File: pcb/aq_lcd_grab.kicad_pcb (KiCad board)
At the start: 4 copper layers, 32 x 50 mm, 39 parts, among them J1 FH26W-39S-0.3SHW(60), J2 FH26W-39S-0.3SHW(60), J3 Conn_01x03_Socket, J4 Conn_01x02_Socket, J5 Conn_01x03_Pin, U1 STM32F103C8T6, U2 Conn_01x14

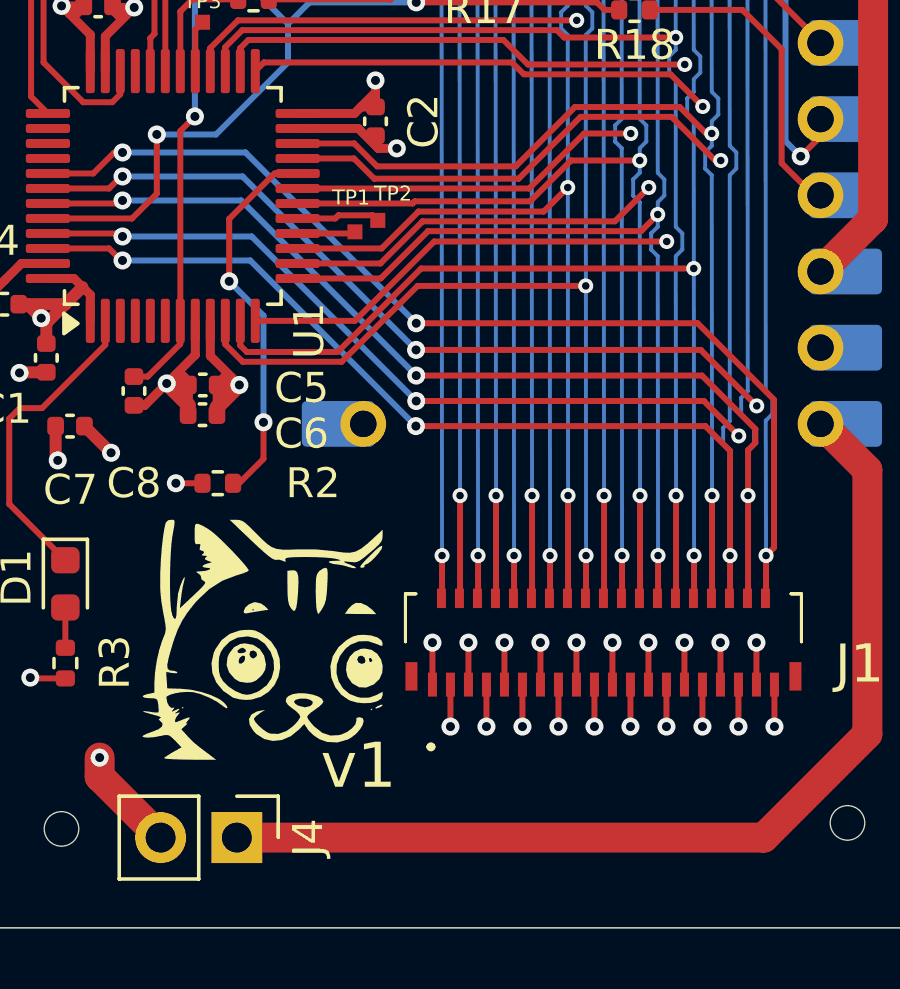
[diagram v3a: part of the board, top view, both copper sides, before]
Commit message: pcb: v2 — fix WR/CS swap on flex pins 22/24
The SKiDL pin map still carried the early probed pinout (22 = WR,
24 = CS); the module datasheet (docs/display_notes.md) has 22 = CS,
24 = WR. v1 therefore clocks TIM2_ETR (PA0) with CS instead of WR.

- aq_lcd_grab.py / .net / route_lcd_bus.py: swap pins 22 and 24.
- kicad_pcb: move the PA0/PA5 tap vias across the pin-22/24 columns,
  mirror the In2.Cu kinks of DC/P21/P25 around the new via spots,
  refill zones, relabel silkscreen v1 -> v2. DRC clean.
- pcb_spec.md: correct pinout table; add "v1 errata" describing the
  bodge wire (J2 "CS" pad -> U1 pin 10/PA0) for built v1 boards.

Co-Authored-By: Claude Opus 5.5 (1M context) <noreply@anthropic.com>
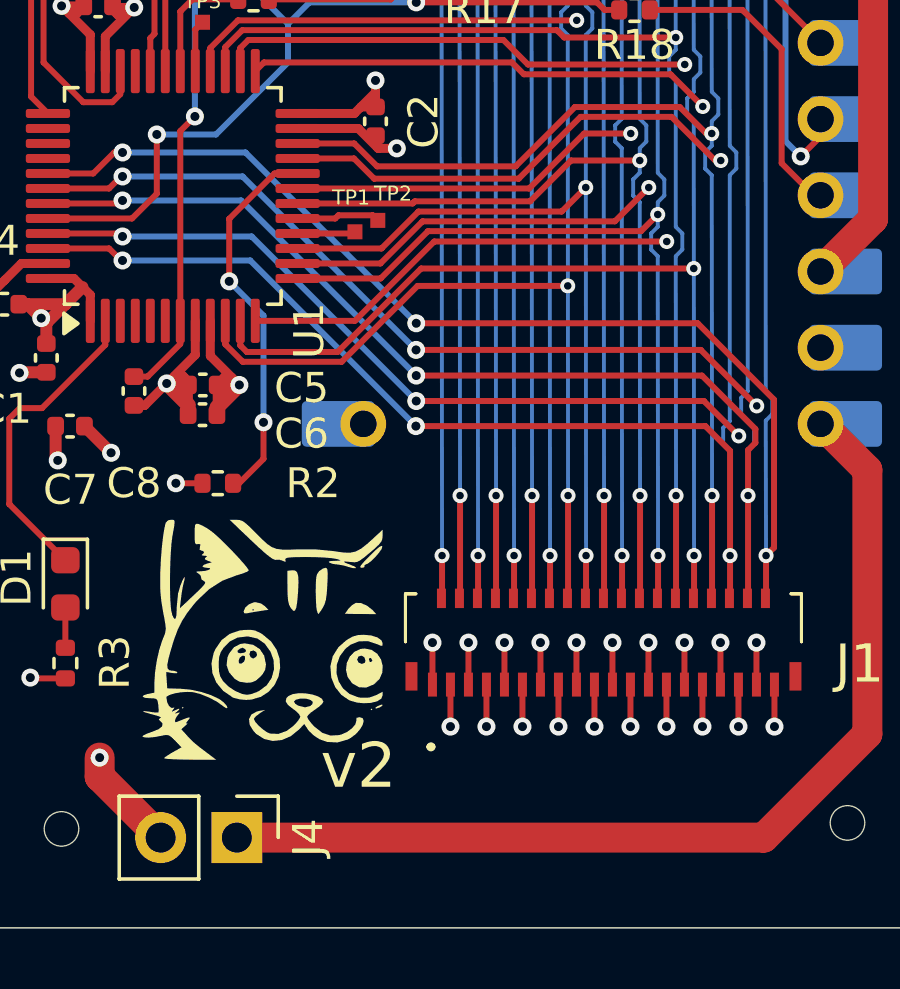
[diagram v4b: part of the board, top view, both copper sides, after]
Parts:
- renumbered v1 to v2
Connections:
- J1 pad 16: CS -> WR
- J1 pad 18: WR -> CS
- J2 pad 22: WR -> CS
- J2 pad 24: CS -> WR
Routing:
- net WR: track 41.1 -> 40.1 mm
- net CS: track 36.5 -> 37.5 mm
